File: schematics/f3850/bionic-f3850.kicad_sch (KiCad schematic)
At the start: 9 parts, among them J1 Bionic-P135, J2 Bionic-P245, U1 F3850, U2 74HCT126, U3 LM78L12, U4 11AA010-I/TO

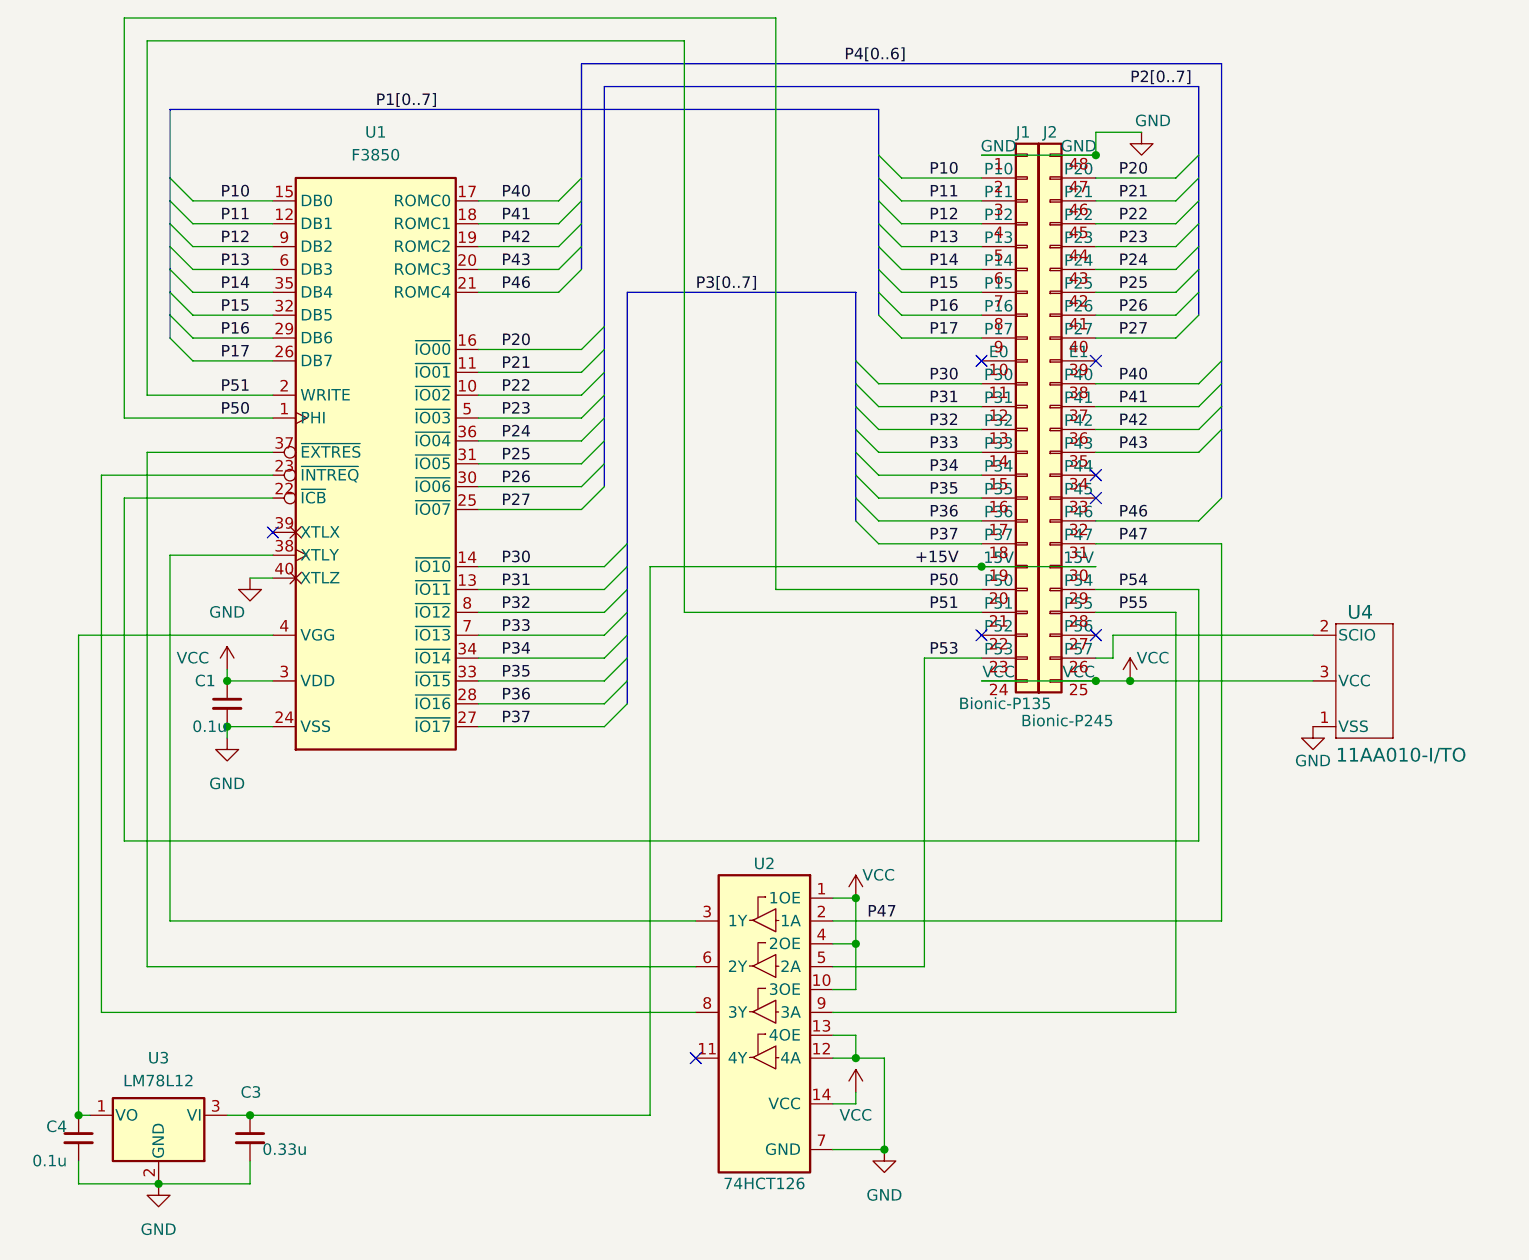
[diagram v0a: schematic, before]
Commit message: [F3850] Move schematics directory
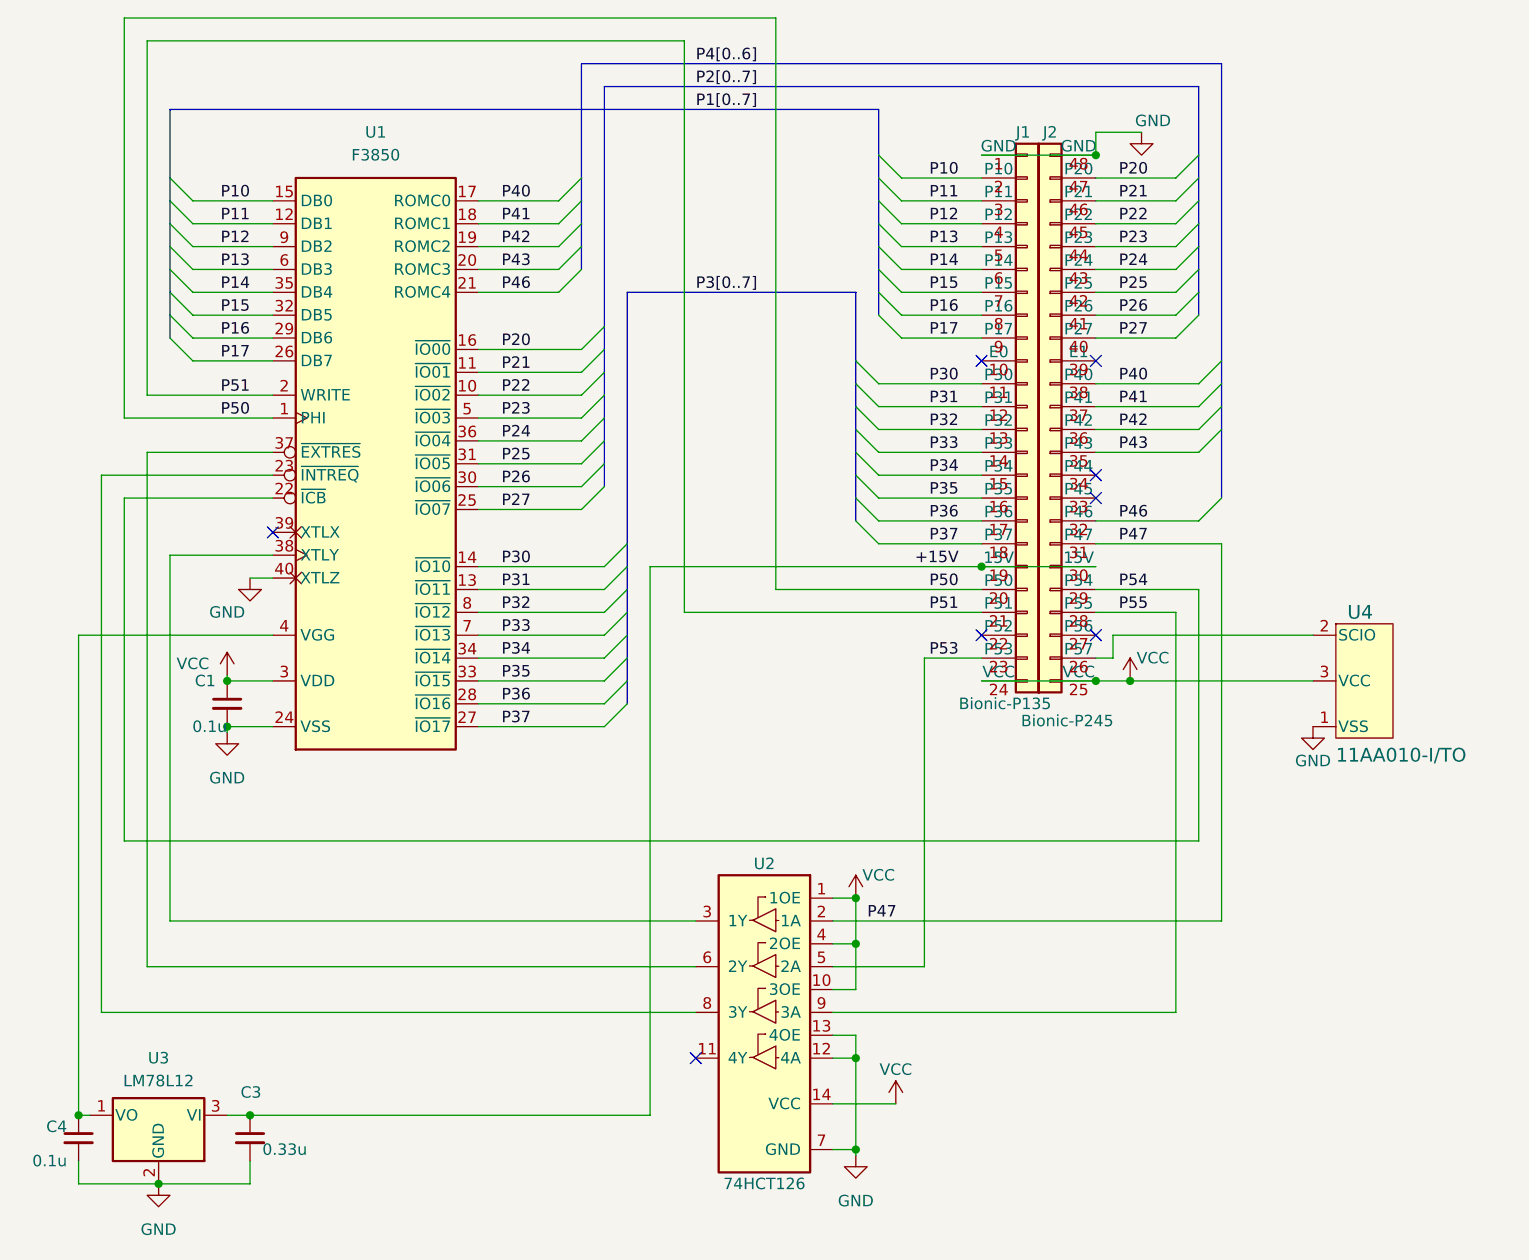
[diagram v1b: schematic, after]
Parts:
- U4: footprint 0-LocalLibrary:TO-92_MC_MCH -> TO-92_MC_MCH
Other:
- title: BionicF3850 Mezzanine -> BionicF3850

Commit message: [F3850] Remove HC126
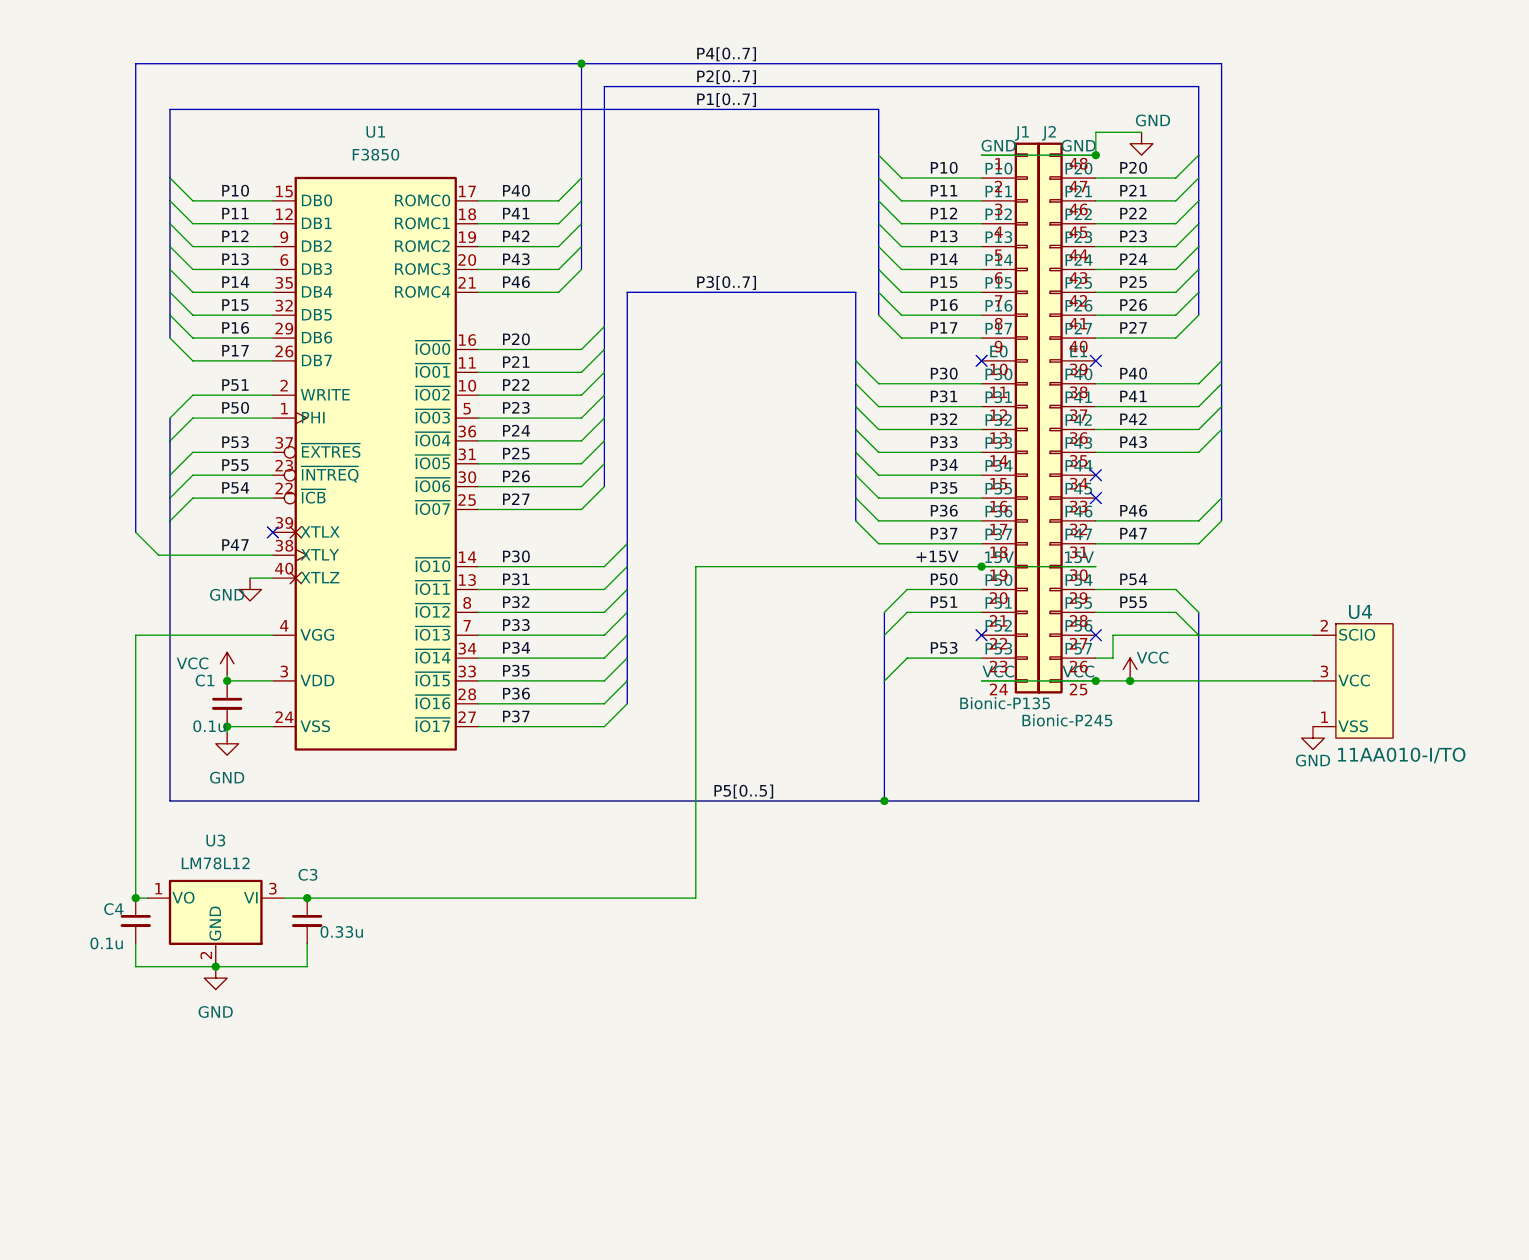
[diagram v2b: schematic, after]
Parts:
- removed U2: 74HCT126, Package_DIP:DIP-14_W7.62mm_Socket, symbol 0-LocalLibrary:74HCT126
- U1: footprint Package_DIP:DIP-40_W15.24mm_Socket -> Package_DIP:DIP-40_W15.24mm
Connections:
- net P47: now also U1.38 (XTLY)
- net P53: now also U1.37 (~{EXTRES})
- net P55: now also U1.23 (~{INTREQ})
- no-connect marks 8 -> 7
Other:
- moved on the sheet: C3, C4, U3
